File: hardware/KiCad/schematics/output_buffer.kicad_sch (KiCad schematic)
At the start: 11 parts, among them U1 MCP6022

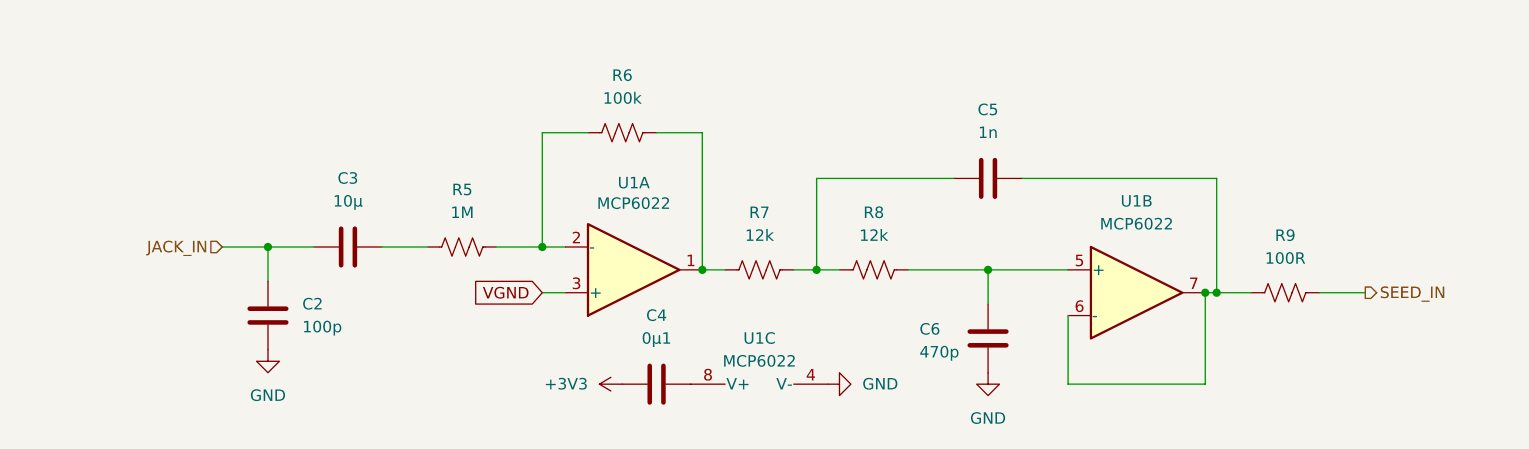
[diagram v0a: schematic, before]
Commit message: Footprint assignments for most components; file organization.
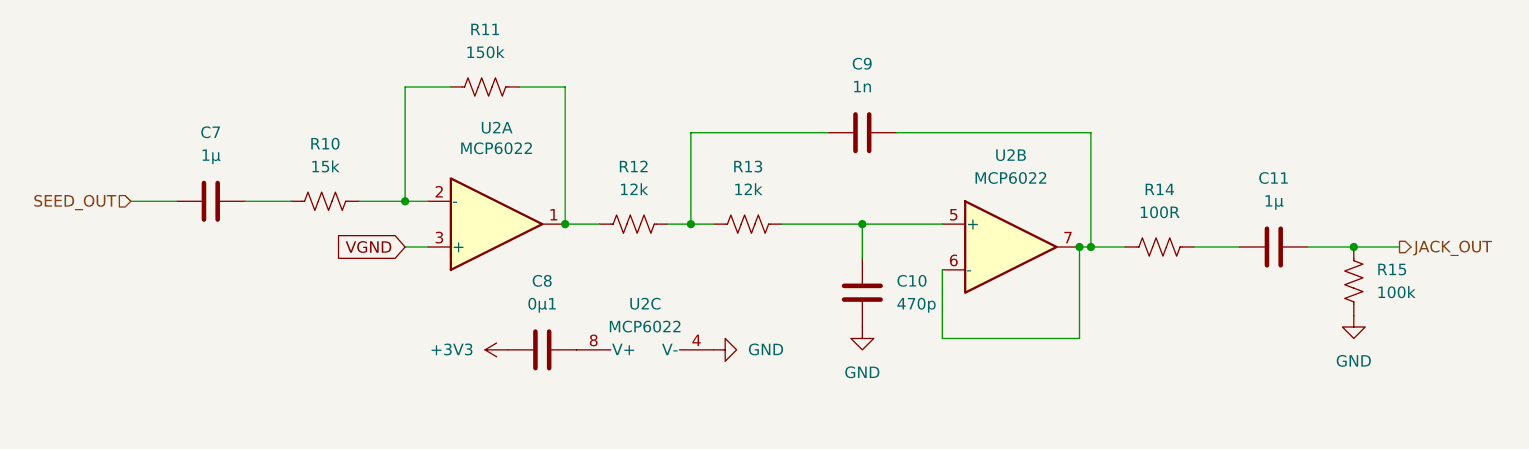
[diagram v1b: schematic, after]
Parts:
- removed C2: 100p, symbol Device:C
- removed C3: 10µ, symbol Device:C
- removed C4: 0µ1, symbol Device:C
- removed C5: 1n, symbol Device:C
- removed C6: 470p, symbol Device:C
- removed R5: 1M, symbol Device:R_US
- removed R6: 100k, symbol Device:R_US
- removed R7, R8: 12k, symbol Device:R_US
- removed R9: 100R, symbol Device:R_US
- removed U1: MCP6022, symbol Amplifier_Operational:MCP6022
- added C10: 470p, Capacitor_THT:C_Rect_L4.0mm_W2.5mm_P2.50mm, symbol Device:C
- added C11, C7: 1µ, Capacitor_THT_Custom:C_Rect_L7.3mm_W4.5mm_P5.00mm, symbol Device:C
- added C8: 0µ1, Capacitor_THT_Custom:C_Rect_L4.0mm_W2.6mm_P2.50mm, symbol Device:C
- added C9: 1n, Capacitor_THT:C_Rect_L4.0mm_W2.5mm_P2.50mm, symbol Device:C
- added R10: 15k, Resistor_THT:R_Axial_DIN0207_L6.3mm_D2.5mm_P7.62mm_Horizontal, symbol Device:R_US
- added R11: 150k, Resistor_THT:R_Axial_DIN0207_L6.3mm_D2.5mm_P7.62mm_Horizontal, symbol Device:R_US
- added R12, R13: 12k, Resistor_THT:R_Axial_DIN0207_L6.3mm_D2.5mm_P7.62mm_Horizontal, symbol Device:R_US
- added R14: 100R, Resistor_THT:R_Axial_DIN0207_L6.3mm_D2.5mm_P7.62mm_Horizontal, symbol Device:R_US
- added R15: 100k, Resistor_THT:R_Axial_DIN0207_L6.3mm_D2.5mm_P7.62mm_Horizontal, symbol Device:R_US
- added U2: MCP6022, Package_DIP:DIP-8_W7.62mm, symbol Amplifier_Operational:MCP6022
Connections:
- net +3V3: now also C8.1
- net GND: now also C10.2, R15.2, U2.4 (V-)
- net VGND: now also U2.3 (+)
- new net: C7.1, R10.1
- new net: R10.2, R11.1, U2.2 (-)
- new net: R11.2, R12.1, U2.1
- new net: C8.2, U2.8 (V+)
- new net: C9.1, R12.2, R13.1
- new net: C10.1, R13.2, U2.5 (+)
- new net: C11.1, R14.2
- new net: C9.2, R14.1, U2.6 (-), U2.7
- new net JACK_OUT: C11.2, R15.1
- new net SEED_OUT: C7.2

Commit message: Added power flags.
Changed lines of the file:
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@@
+		(color 0 0 0 0)
+	)
+	(junction
+		(at 124.46 111.76)
+		(diameter 0)
 		(color 0 0 0 0)
 	)
@@
 					(unit 1)
 				)
+			)
+		)
+	)
+	(symbol
+		(lib_id "power:PWR_FLAG")
+		(at 124.46 111.76 180)
+		(unit 1)
+		(body_style 1)
+		(exclude_from_sim no)
+		(in_bom yes)
+		(on_board yes)
+		(in_pos_files yes)
+		(dnp no)
+		(fields_autoplaced yes)
+		(property "Reference" "#FLG05"
+			(at 124.46 113.665 0)
+			(hide yes)
+			(show_name no)
+			(do_not_autoplace no)
+			(effects
+				(font
+					(size 1.27 1.27)
+				)
+			)
+		)
+		(property "Value" "PWR_FLAG"
+			(at 124.46 116.84 0)
+			(show_name no)
+			(do_not_autoplace no)
+			(effects
+				(font
+					(size 1.27 1.27)
+				)
+			)
+		)
+		(property "Footprint" ""
+			(at 124.46 111.76 0)
+			(hide yes)
+			(show_name no)
+			(do_not_autoplace no)
+			(effects
+				(font
+					(size 1.27 1.27)
+				)
+			)
+		)
+		(property "Datasheet" ""
+			(at 124.46 111.76 0)
+			(hide yes)
+			(show_name no)
+			(do_not_autoplace no)
+			(effects
+				(font
+					(size 1.27 1.27)
+				)
+			)
+		)
+		(property "Description" "Special symbol for telling ERC where power comes from"
+			(at 124.46 111.76 0)
+			(hide yes)
+			(show_name no)
+			(do_not_autoplace no)
+			(effects
+				(font
+					(size 1.27 1.27)
+				)
+			)
+		)
+		(pin "1"
+		)
+		(instances
+			(project "freq-fiche"
+				(path "/fc444d3c-3a1a-4715-bcff-119f4d2b4d9e/cb3a069d-198c-4da3-9ecb-baa625ac1fdd"
+					(reference "#FLG05")
+					(unit 1)
+				)

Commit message: Power conditioning.
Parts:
- C8: value 0µ1 -> 100n
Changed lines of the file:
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@@
 			)
 		)
-		(property "Value" "0µ1"
+		(property "Value" "100n"
 			(at 120.65 106.68 90)
 			(show_name no)
@@
 		(in_pos_files yes)
 		(dnp no)
-		(fields_autoplaced yes)
 		(property "Reference" "C10"
-			(at 160.02 104.1399 0)
+			(at 147.828 104.394 0)
 			(show_name no)
 			(do_not_autoplace no)
@@
 		)
 		(property "Value" "470p"
-			(at 160.02 106.6799 0)
-			(show_name no)
-			(do_not_autoplace no)
+			(at 147.828 106.934 0)
+			(show_name no)
+			(do_not_autoplace no)

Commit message: Gain staging; source pin reassignments.
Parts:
- R10: value 15k -> 33k
- R11: value 150k -> 22k
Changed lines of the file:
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@@
 			)
 		)
-		(property "Value" "15k"
+		(property "Value" "33k"
 			(at 96.52 91.44 90)
 			(show_name no)
@@
 			)
 		)
-		(property "Value" "150k"
+		(property "Value" "22k"
 			(at 114.3 78.74 90)
 			(show_name no)
